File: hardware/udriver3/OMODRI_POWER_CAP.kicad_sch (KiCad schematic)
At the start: 9 parts, among them J13 Conn_01x02

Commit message: Update all files and lib to use new kicad 6 format
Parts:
- D11: footprint udriver3:D_0201_0603Metric -> Diode_SMD:D_0201_0603Metric
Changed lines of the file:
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@@
       (effects (font (size 1.27 1.27)) hide)
     )
-    (property "Datasheet" "https://product.tdk.com/info/en/catalog/datasheets/mlcc_commercial_midvoltage_en.pdf" (id 3) (at 121.92 104.14 0)
+    (property "Datasheet" "~" (id 3) (at 121.92 104.14 0)
       (effects (font (size 1.27 1.27)) hide)
     )
@@
       (effects (font (size 1.27 1.27)) hide)
     )
-    (property "Datasheet" "https://product.tdk.com/info/en/catalog/datasheets/mlcc_commercial_midvoltage_en.pdf" (id 3) (at 130.81 104.14 0)
+    (property "Datasheet" "~" (id 3) (at 130.81 104.14 0)
       (effects (font (size 1.27 1.27)) hide)
     )
@@
       (effects (font (size 1.27 1.27)) hide)
     )
-    (property "Datasheet" "https://product.tdk.com/info/en/catalog/datasheets/mlcc_commercial_midvoltage_en.pdf" (id 3) (at 139.7 104.14 0)
+    (property "Datasheet" "~" (id 3) (at 139.7 104.14 0)
       (effects (font (size 1.27 1.27)) hide)
     )
@@
       (effects (font (size 1.27 1.27)) (justify left))
     )
-    (property "Footprint" "udriver3:D_0201_0603Metric" (id 2) (at 188.595 104.14 0)
+    (property "Footprint" "Diode_SMD:D_0201_0603Metric" (id 2) (at 188.595 104.14 0)
       (effects (font (size 1.27 1.27)) hide)
     )
@@
       (effects (font (size 1.27 1.27)) hide)
     )
-    (property "Datasheet" "https://www.murata.com/en-eu/products/productdetail?partno=GRM033R71E103KE14%23" (id 3) (at 167.005 109.22 0)
+    (property "Datasheet" "~" (id 3) (at 167.005 109.22 0)
       (effects (font (size 1.27 1.27)) hide)
     )
@@
       (effects (font (size 1.27 1.27)) hide)
     )
-    (property "Datasheet" "https://industrial.panasonic.com/cdbs/www-data/pdf/RDA0000/AOA0000C304.pdf" (id 3) (at 158.115 109.22 0)
+    (property "Datasheet" "~" (id 3) (at 158.115 109.22 0)
       (effects (font (size 1.27 1.27)) hide)
     )
@@
       (effects (font (size 1.27 1.27)) hide)
     )
-    (property "Datasheet" "https://industrial.panasonic.com/cdbs/www-data/pdf/RDA0000/AOA0000C304.pdf" (id 3) (at 158.115 99.06 0)
+    (property "Datasheet" "~" (id 3) (at 158.115 99.06 0)
       (effects (font (size 1.27 1.27)) hide)
     )
@@
       (effects (font (size 1.27 1.27)) hide)
     )
-    (property "Datasheet" "https://www.tme.eu/en/Document/ce4077e36b79046da520ca73227e15de/XT30PW%20SPEC.pdf" (id 3) (at 107.95 105.41 0)
+    (property "Datasheet" "~" (id 3) (at 107.95 105.41 0)
       (effects (font (size 1.27 1.27)) hide)
     )
@@
       (effects (font (size 1.27 1.27)) hide)
     )
-    (property "Datasheet" "https://product.tdk.com/info/en/catalog/datasheets/mlcc_commercial_midvoltage_en.pdf" (id 3) (at 148.59 104.14 0)
-      (effects (font (size 1.27 1.27)) hide)
-    )
+    (property "Datasheet" "~" (id 3) (at 148.59 104.14 0)
+      (effects (font (size 1.27 1.27)) hide)
+    )

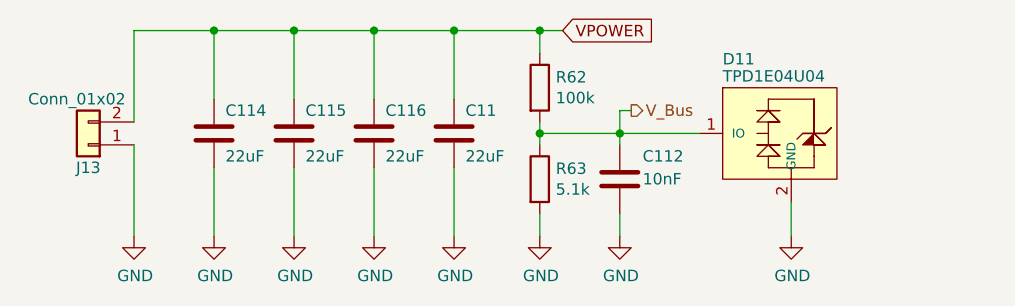
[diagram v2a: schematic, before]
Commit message: Temporary version of udrive3 v2.0. - In schematic there are 2 solutions for DC/DC buck converter. - PCB routing is not finished yet.
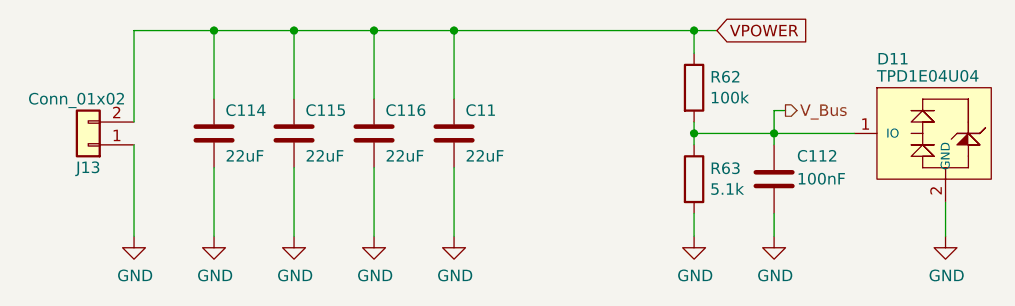
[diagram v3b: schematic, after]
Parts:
- C112: value 10nF -> 100nF; DigiKey 490-14454-1-ND -> 490-14571-1-ND; Farnell 2990696 -> 3790414; Mouser 81-GRM033R71E103KE4D -> 81-GRM033R61E104KE4J; Part No GRM033R71E103KE14D -> GRM033R61E104KE14J; RS 185-2059 -> 185-2066
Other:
- moved on the sheet: C112, D11, R62, R63

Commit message: PCB update. Re-annotation of the design + via stitching (GND).
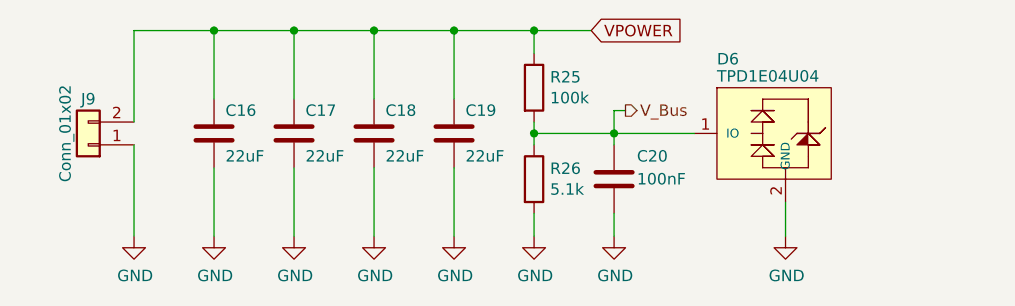
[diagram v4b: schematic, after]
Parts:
- renumbered C114 to C16, C115 to C17, C116 to C18, C11 to C19, C112 to C20, D11 to D6, J13 to J9, R62 to R25, R63 to R26
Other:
- moved on the sheet: C20, D6, R25, R26

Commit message: PCB updates - FSI protection added against FPC cable reverse connection - BOSCH BMI088 IMU added.
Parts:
- D7: renamed from D6; footprint Diode_SMD:D_0201_0603Metric -> Diode_SMD:D_0402_1005Metric
- renumbered C16 to C17, C17 to C18, C18 to C19, C19 to C20, C20 to C21, R25 to R26, R26 to R27
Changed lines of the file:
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@@
   (title_block
     (title "Open MOtor DRiver Initiative (OMODRI)")
-    (date "2022-10-05")
+    (date "2022-11-24")
     (rev "2.0")
     (company "LAAS/CNRS")
@@
   (symbol (lib_id "Device:C") (at 121.92 104.14 0) (unit 1)
     (in_bom yes) (on_board yes)
-    (property "Reference" "C16" (id 0) (at 123.19 101.6 0)
+    (property "Reference" "C17" (id 0) (at 123.19 101.6 0)
       (effects (font (size 1.27 1.27)) (justify left))
     )
@@
   (symbol (lib_id "Device:C") (at 130.81 104.14 0) (unit 1)
     (in_bom yes) (on_board yes)
-    (property "Reference" "C17" (id 0) (at 132.08 101.6 0)
+    (property "Reference" "C18" (id 0) (at 132.08 101.6 0)
       (effects (font (size 1.27 1.27)) (justify left))
     )
@@
   (symbol (lib_id "Device:C") (at 139.7 104.14 0) (unit 1)
     (in_bom yes) (on_board yes)
-    (property "Reference" "C18" (id 0) (at 140.97 101.6 0)
+    (property "Reference" "C19" (id 0) (at 140.97 101.6 0)
       (effects (font (size 1.27 1.27)) (justify left))
     )
@@
   (symbol (lib_id "power:GND") (at 185.42 115.57 0) (unit 1)
     (in_bom yes) (on_board yes)
-    (property "Reference" "#PWR075" (id 0) (at 185.42 121.92 0)
+    (property "Reference" "#PWR076" (id 0) (at 185.42 121.92 0)
       (effects (font (size 1.27 1.27)) hide)
     )
@@
   (symbol (lib_id "omodri_lib:TPD1E04U04") (at 185.42 104.14 0) (unit 1)
     (in_bom yes) (on_board yes)
-    (property "Reference" "D6" (id 0) (at 177.8 95.885 0)
+    (property "Reference" "D7" (id 0) (at 177.8 95.885 0)
       (effects (font (size 1.27 1.27)) (justify left))
     )
@@
       (effects (font (size 1.27 1.27)) (justify left))
     )
-    (property "Footprint" "Diode_SMD:D_0201_0603Metric" (id 2) (at 187.96 104.14 0)
+    (property "Footprint" "Diode_SMD:D_0402_1005Metric" (id 2) (at 187.96 104.14 0)
       (effects (font (size 1.27 1.27)) hide)
     )
@@
   (symbol (lib_id "power:GND") (at 166.37 115.57 0) (unit 1)
     (in_bom yes) (on_board yes)
-    (property "Reference" "#PWR074" (id 0) (at 166.37 121.92 0)
+    (property "Reference" "#PWR075" (id 0) (at 166.37 121.92 0)
       (effects (font (size 1.27 1.27)) hide)
     )
@@
   (symbol (lib_id "power:GND") (at 113.03 115.57 0) (unit 1)
     (in_bom yes) (on_board yes)
-    (property "Reference" "#PWR068" (id 0) (at 113.03 121.92 0)
+    (property "Reference" "#PWR069" (id 0) (at 113.03 121.92 0)
       (effects (font (size 1.27 1.27)) hide)
     )
@@
   (symbol (lib_id "Device:C") (at 166.37 109.22 0) (unit 1)
     (in_bom yes) (on_board yes)
-    (property "Reference" "C20" (id 0) (at 168.91 106.68 0)
+    (property "Reference" "C21" (id 0) (at 168.91 106.68 0)
       (effects (font (size 1.27 1.27)) (justify left))
     )
@@
   (symbol (lib_id "Device:R") (at 157.48 109.22 0) (unit 1)
     (in_bom yes) (on_board yes)
-    (property "Reference" "R26" (id 0) (at 159.258 108.0516 0)
+    (property "Reference" "R27" (id 0) (at 159.258 108.0516 0)
       (effects (font (size 1.27 1.27)) (justify left))
     )
@@
   (symbol (lib_id "Device:R") (at 157.48 99.06 0) (unit 1)
     (in_bom yes) (on_board yes)
-    (property "Reference" "R25" (id 0) (at 159.258 97.8916 0)
+    (property "Reference" "R26" (id 0) (at 159.258 97.8916 0)
       (effects (font (size 1.27 1.27)) (justify left))
     )
@@
   (symbol (lib_id "power:GND") (at 157.48 115.57 0) (unit 1)
     (in_bom yes) (on_board yes)
-    (property "Reference" "#PWR073" (id 0) (at 157.48 121.92 0)
+    (property "Reference" "#PWR074" (id 0) (at 157.48 121.92 0)
       (effects (font (size 1.27 1.27)) hide)
     )
@@
   (symbol (lib_id "power:GND") (at 139.7 115.57 0) (unit 1)
     (in_bom yes) (on_board yes)
-    (property "Reference" "#PWR071" (id 0) (at 139.7 121.92 0)
+    (property "Reference" "#PWR072" (id 0) (at 139.7 121.92 0)
       (effects (font (size 1.27 1.27)) hide)
     )
@@
   (symbol (lib_id "power:GND") (at 130.81 115.57 0) (unit 1)
     (in_bom yes) (on_board yes)
-    (property "Reference" "#PWR070" (id 0) (at 130.81 121.92 0)
+    (property "Reference" "#PWR071" (id 0) (at 130.81 121.92 0)
       (effects (font (size 1.27 1.27)) hide)
     )
@@
   (symbol (lib_id "power:GND") (at 121.92 115.57 0) (unit 1)
     (in_bom yes) (on_board yes)
-    (property "Reference" "#PWR069" (id 0) (at 121.92 121.92 0)
+    (property "Reference" "#PWR070" (id 0) (at 121.92 121.92 0)
       (effects (font (size 1.27 1.27)) hide)
     )
@@
   (symbol (lib_id "Device:C") (at 148.59 104.14 0) (unit 1)
     (in_bom yes) (on_board yes)
-    (property "Reference" "C19" (id 0) (at 149.86 101.6 0)
+    (property "Reference" "C20" (id 0) (at 149.86 101.6 0)
       (effects (font (size 1.27 1.27)) (justify left))
     )
@@
   (symbol (lib_id "power:GND") (at 148.59 115.57 0) (unit 1)
     (in_bom yes) (on_board yes)
-    (property "Reference" "#PWR072" (id 0) (at 148.59 121.92 0)
-      (effects (font (size 1.27 1.27)) hide)
-    )
+    (property "Reference" "#PWR073" (id 0) (at 148.59 121.92 0)
+      (effects (font (size 1.27 1.27)) hide)
+    )

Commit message: PCB udpates. - add serial resistors on boot jumpers - modify config jumpers to be opened by default
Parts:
- renumbered C17 to C15, C18 to C16, C19 to C17, C20 to C18, C21 to C19, D7 to D5, J9 to J6, R26 to R24, R27 to R25
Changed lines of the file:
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@@
   (symbol (lib_id "Device:C") (at 121.92 104.14 0) (unit 1)
     (in_bom yes) (on_board yes)
-    (property "Reference" "C17" (id 0) (at 123.19 101.6 0)
+    (property "Reference" "C15" (id 0) (at 123.19 101.6 0)
       (effects (font (size 1.27 1.27)) (justify left))
     )
@@
   (symbol (lib_id "Device:C") (at 130.81 104.14 0) (unit 1)
     (in_bom yes) (on_board yes)
-    (property "Reference" "C18" (id 0) (at 132.08 101.6 0)
+    (property "Reference" "C16" (id 0) (at 132.08 101.6 0)
       (effects (font (size 1.27 1.27)) (justify left))
     )
@@
   (symbol (lib_id "Device:C") (at 139.7 104.14 0) (unit 1)
     (in_bom yes) (on_board yes)
-    (property "Reference" "C19" (id 0) (at 140.97 101.6 0)
+    (property "Reference" "C17" (id 0) (at 140.97 101.6 0)
       (effects (font (size 1.27 1.27)) (justify left))
     )
@@
   (symbol (lib_id "power:GND") (at 185.42 115.57 0) (unit 1)
     (in_bom yes) (on_board yes)
-    (property "Reference" "#PWR076" (id 0) (at 185.42 121.92 0)
+    (property "Reference" "#PWR062" (id 0) (at 185.42 121.92 0)
       (effects (font (size 1.27 1.27)) hide)
     )
@@
   (symbol (lib_id "omodri_lib:TPD1E04U04") (at 185.42 104.14 0) (unit 1)
     (in_bom yes) (on_board yes)
-    (property "Reference" "D7" (id 0) (at 177.8 95.885 0)
+    (property "Reference" "D5" (id 0) (at 177.8 95.885 0)
       (effects (font (size 1.27 1.27)) (justify left))
     )
@@
   (symbol (lib_id "power:GND") (at 166.37 115.57 0) (unit 1)
     (in_bom yes) (on_board yes)
-    (property "Reference" "#PWR075" (id 0) (at 166.37 121.92 0)
+    (property "Reference" "#PWR061" (id 0) (at 166.37 121.92 0)
       (effects (font (size 1.27 1.27)) hide)
     )
@@
   (symbol (lib_id "power:GND") (at 113.03 115.57 0) (unit 1)
     (in_bom yes) (on_board yes)
-    (property "Reference" "#PWR069" (id 0) (at 113.03 121.92 0)
+    (property "Reference" "#PWR055" (id 0) (at 113.03 121.92 0)
       (effects (font (size 1.27 1.27)) hide)
     )
@@
   (symbol (lib_id "Device:C") (at 166.37 109.22 0) (unit 1)
     (in_bom yes) (on_board yes)
-    (property "Reference" "C21" (id 0) (at 168.91 106.68 0)
+    (property "Reference" "C19" (id 0) (at 168.91 106.68 0)
       (effects (font (size 1.27 1.27)) (justify left))
     )
@@
   (symbol (lib_id "Device:R") (at 157.48 109.22 0) (unit 1)
     (in_bom yes) (on_board yes)
-    (property "Reference" "R27" (id 0) (at 159.258 108.0516 0)
+    (property "Reference" "R25" (id 0) (at 159.258 108.0516 0)
       (effects (font (size 1.27 1.27)) (justify left))
     )
@@
   (symbol (lib_id "Device:R") (at 157.48 99.06 0) (unit 1)
     (in_bom yes) (on_board yes)
-    (property "Reference" "R26" (id 0) (at 159.258 97.8916 0)
+    (property "Reference" "R24" (id 0) (at 159.258 97.8916 0)
       (effects (font (size 1.27 1.27)) (justify left))
     )
@@
   (symbol (lib_id "Connector_Generic:Conn_01x02") (at 107.95 105.41 180) (unit 1)
     (in_bom yes) (on_board yes)
-    (property "Reference" "J9" (id 0) (at 107.95 100.33 0))
+    (property "Reference" "J6" (id 0) (at 107.95 100.33 0))
     (property "Value" "Conn_01x02" (id 1) (at 105.41 104.14 90))
     (property "Footprint" "udriver3:AMASS_XT30PW-M_1x02_P2.50mm_Horizontal" (id 2) (at 107.95 105.41 0)
@@
   (symbol (lib_id "power:GND") (at 157.48 115.57 0) (unit 1)
     (in_bom yes) (on_board yes)
-    (property "Reference" "#PWR074" (id 0) (at 157.48 121.92 0)
+    (property "Reference" "#PWR060" (id 0) (at 157.48 121.92 0)
       (effects (font (size 1.27 1.27)) hide)
     )
@@
   (symbol (lib_id "power:GND") (at 139.7 115.57 0) (unit 1)
     (in_bom yes) (on_board yes)
-    (property "Reference" "#PWR072" (id 0) (at 139.7 121.92 0)
+    (property "Reference" "#PWR058" (id 0) (at 139.7 121.92 0)
       (effects (font (size 1.27 1.27)) hide)
     )
@@
   (symbol (lib_id "power:GND") (at 130.81 115.57 0) (unit 1)
     (in_bom yes) (on_board yes)
-    (property "Reference" "#PWR071" (id 0) (at 130.81 121.92 0)
+    (property "Reference" "#PWR057" (id 0) (at 130.81 121.92 0)
       (effects (font (size 1.27 1.27)) hide)
     )
@@
   (symbol (lib_id "power:GND") (at 121.92 115.57 0) (unit 1)
     (in_bom yes) (on_board yes)
-    (property "Reference" "#PWR070" (id 0) (at 121.92 121.92 0)
+    (property "Reference" "#PWR056" (id 0) (at 121.92 121.92 0)
       (effects (font (size 1.27 1.27)) hide)
     )
@@
   (symbol (lib_id "Device:C") (at 148.59 104.14 0) (unit 1)
     (in_bom yes) (on_board yes)
-    (property "Reference" "C20" (id 0) (at 149.86 101.6 0)
+    (property "Reference" "C18" (id 0) (at 149.86 101.6 0)
       (effects (font (size 1.27 1.27)) (justify left))
     )
@@
   (symbol (lib_id "power:GND") (at 148.59 115.57 0) (unit 1)
     (in_bom yes) (on_board yes)
-    (property "Reference" "#PWR073" (id 0) (at 148.59 121.92 0)
-      (effects (font (size 1.27 1.27)) hide)
-    )
+    (property "Reference" "#PWR059" (id 0) (at 148.59 121.92 0)
+      (effects (font (size 1.27 1.27)) hide)
+    )

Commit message: First release of uOmodri v3. Swap COM SPI. Modify CAN to CAN FD and bus sharing with RS485.
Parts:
- C15, C16, C17, C18: footprint Capacitor_SMD:C_2220_5650Metric -> Capacitor_SMD:C_2220_5750Metric

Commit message: Modify JP5/JP6 jumper to remove DRC error. Add gate resistor on power MOSFET (high & low side).
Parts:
- J6: Part No (none) -> XT30PW-M; RS (none) -> 180-5359
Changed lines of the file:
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@@
     (title "Open MOtor DRiver Initiative (OMODRI)")
     (date "2022-11-24")
-    (rev "2.0")
+    (rev "3.0")
     (company "LAAS/CNRS")
   )
@@
       (effects (font (size 1.27 1.27)) hide)
     )
-    (property "Datasheet" "~" (at 157.48 109.22 0)
+    (property "Datasheet" "https://industrial.panasonic.com/cdbs/www-data/pdf/RDA0000/AOA0000C304.pdf" (at 157.48 109.22 0)
       (effects (font (size 1.27 1.27)) hide)
     )
@@
       (effects (font (size 1.27 1.27)) hide)
     )
-    (property "Datasheet" "~" (at 157.48 99.06 0)
+    (property "Datasheet" "https://industrial.panasonic.com/cdbs/www-data/pdf/RDA0000/AOA0000C304.pdf" (at 157.48 99.06 0)
       (effects (font (size 1.27 1.27)) hide)
     )
@@
       (effects (font (size 1.27 1.27)) hide)
     )
-    (property "Datasheet" "~" (at 107.95 105.41 0)
-      (effects (font (size 1.27 1.27)) hide)
-    )
+    (property "Datasheet" "https://www.tme.eu/Document/6eb2005a51a52592b3f19e8a450c54c8/XT30PW-M.pdf" (at 107.95 105.41 0)
+      (effects (font (size 1.27 1.27)) hide)
+    )
+    (property "RS" "180-5359" (at 107.95 105.41 0)
+      (effects (font (size 1.27 1.27)) hide)
+    )
+    (property "Part No" "XT30PW-M" (at 107.95 105.41 0)
+      (effects (font (size 1.27 1.27)) hide)
+    )
